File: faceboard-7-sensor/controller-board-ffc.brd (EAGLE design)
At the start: 51 x 42 mm, 7 parts, among them J1 DCJ0202

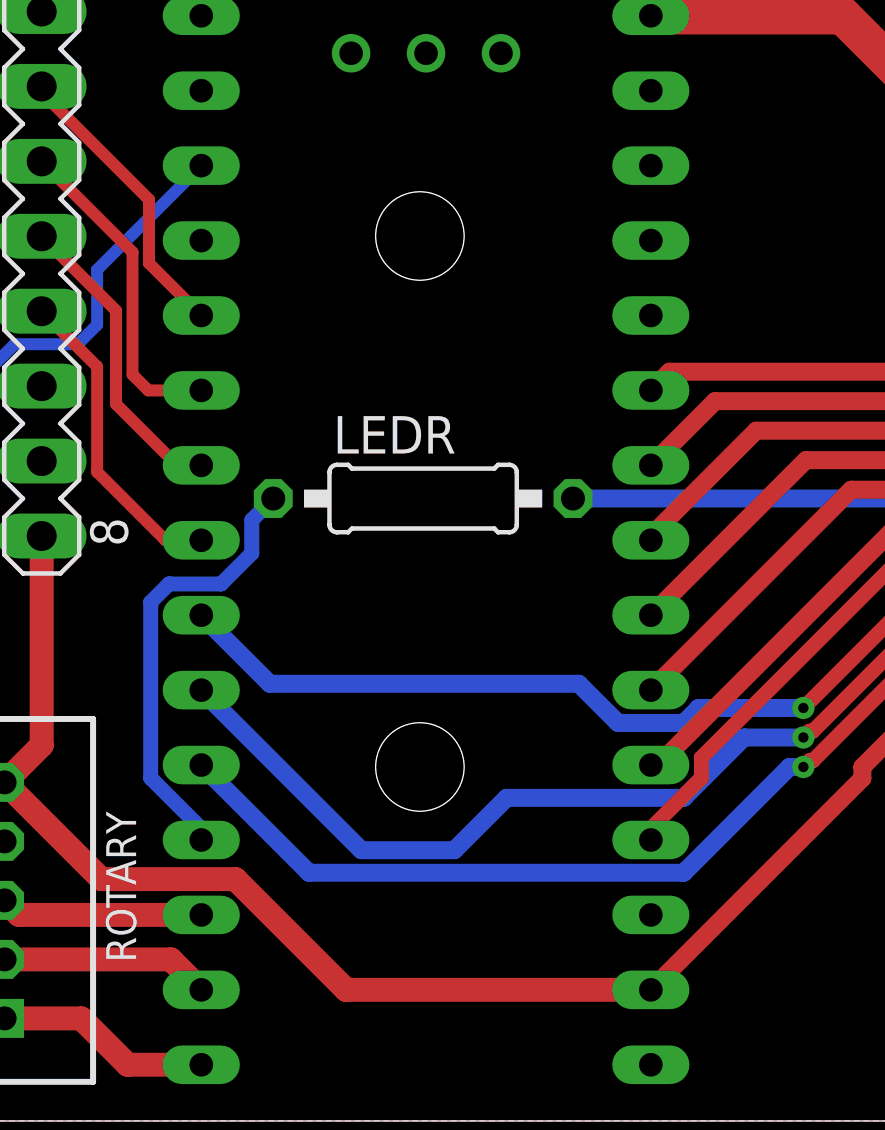
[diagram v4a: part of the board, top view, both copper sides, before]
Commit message: tidy silk screen
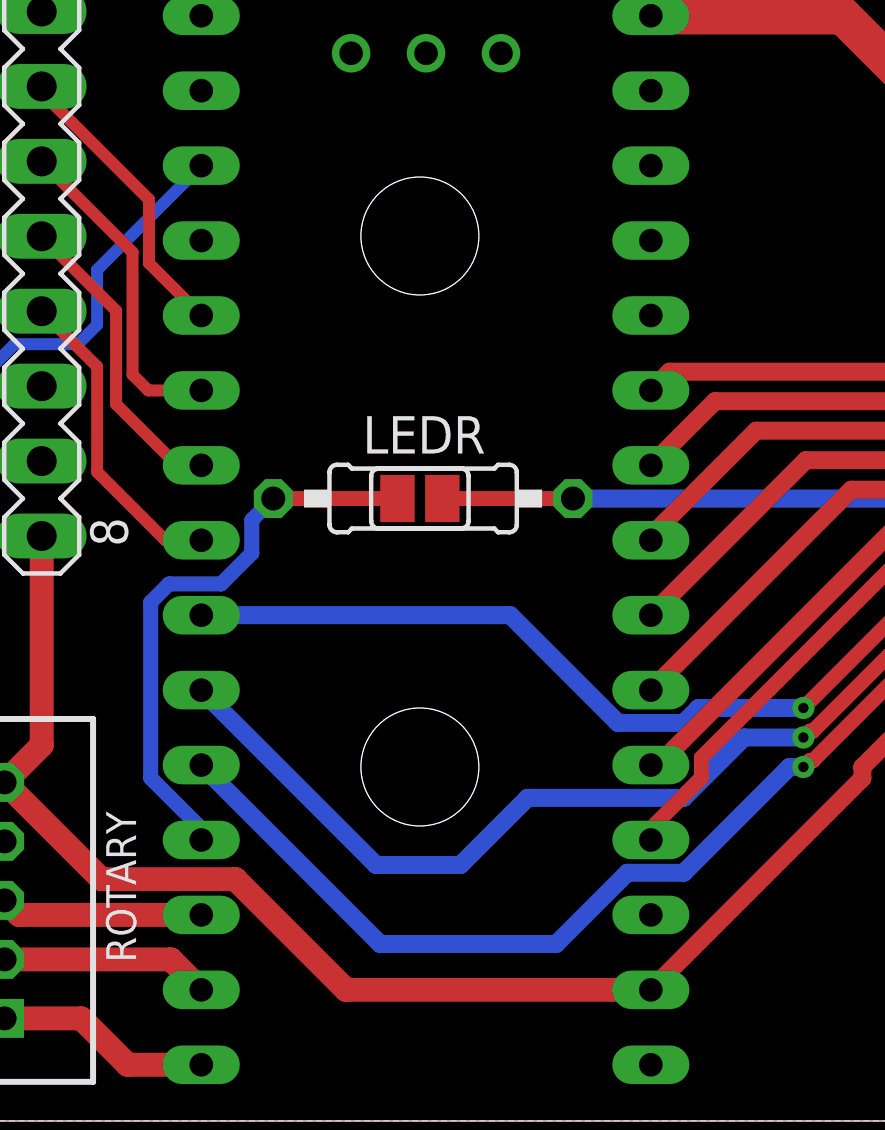
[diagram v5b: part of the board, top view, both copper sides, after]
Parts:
- added SJ1: (no value), jumper:SJ
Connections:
- net D9: now also SJ1.1
- net DIN: now also SJ1.2
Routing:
- net DIN: track 18.8 -> 23.2 mm
- net D9: track 15.0 -> 19.2 mm
- net A: track 29.0 -> 31.0 mm
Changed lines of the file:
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@@
 <layer number="97" name="Info" color="7" fill="1" visible="no" active="no"/>
 <layer number="98" name="Guide" color="6" fill="1" visible="no" active="no"/>
-<layer number="200" name="200bmp" color="1" fill="10" visible="yes" active="yes"/>
-<layer number="201" name="201bmp" color="2" fill="10" visible="yes" active="yes"/>
+<layer number="200" name="tBmp" color="1" fill="10" visible="yes" active="yes"/>
+<layer number="201" name="bBmp" color="2" fill="10" visible="yes" active="yes"/>
 <layer number="250" name="Descript" color="7" fill="1" visible="yes" active="yes"/>
 <layer number="251" name="SMDround" color="7" fill="1" visible="yes" active="yes"/>
@@
 <rectangle x1="1.005140625" y1="41.132178125" x2="8.004140625" y2="41.186859375" layer="201" rot="R180"/>
 <text x="21.7230375" y="1.03151875" size="0.5" layer="26" font="vector" rot="MR180">NEMUS Controller Board v0.1.3</text>
-<hole x="26" y="30" drill="3"/>
-<hole x="26" y="12" drill="3"/>
+<hole x="26" y="30" drill="4"/>
+<hole x="26" y="12" drill="4"/>
 </plain>
 <attributes>
@@
 <attribute name="OC_NEWARK" value="unknown" x="-30" y="-17" size="1.778" layer="27" rot="R270" display="off"/>
 <attribute name="POPULARITY" value="10" x="-30" y="-17" size="1.778" layer="27" rot="R270" display="off"/>
-<attribute name="VALUE" x="7.259" y="32.99" size="1.27" layer="27" ratio="10" rot="R270"/>
 </element>
 <element name="LEDR" library="rcl" library_urn="urn:adsk.eagle:library:334" package="0207/10" package3d_urn="urn:adsk.eagle:package:23491/2" value="300" x="26.11" y="21.1" smashed="yes">
-<attribute name="NAME" x="23.062" y="22.624" size="1.27" layer="25" ratio="10"/>
+<attribute name="NAME" x="24.062" y="22.624" size="1.27" layer="25" ratio="10"/>
 <attribute name="POPULARITY" value="81" x="60.4" y="-42.4" size="1.778" layer="27" display="off"/>
 <attribute name="SPICEPREFIX" value="R" x="60.4" y="-42.4" size="1.778" layer="27" display="off"/>
-<attribute name="VALUE" x="23.8494" y="20.465" size="1.27" layer="27" ratio="10"/>
 </element>
 <element name="ROTARY" library="con-jst-ph" package="B5B-PH-K" value="B5B-PH-K" x="11.921" y="7.477" smashed="yes" rot="R90">
 <attribute name="LABEL" value="" x="16.366" y="1.508" size="1.016" layer="25" ratio="18" rot="R90"/>
 <attribute name="NAME" x="15.365" y="10.492" size="1.016" layer="25" ratio="18" rot="R270"/>
-<attribute name="VALUE" x="13.826" y="2.397" size="1.016" layer="27" ratio="10" rot="R90"/>
 </element>
 <element name="U$1" library="Arduino-clone" package="NANO" value="NANO" x="23.669" y="28.575" smashed="yes" rot="R180"/>
@@
 <attribute name="MOUSER_PRICE-STOCK" value="https://www.mouser.co.uk/ProductDetail/Wurth-Elektronik/686114148922?qs=a9WhcLg8qCz0mPj5zZqo5g%3D%3D" x="46.2" y="18.9" size="1.778" layer="27" rot="R90" display="off"/>
 <attribute name="NAME" x="45.7" y="18.9" size="1.27" layer="25" rot="R90" align="center"/>
-<attribute name="VALUE" x="47.7" y="18.9" size="1.27" layer="27" rot="R90" align="center"/>
 </element>
 <element name="J1" library="con-jack" library_urn="urn:adsk.eagle:library:154" package="DCJ0202" package3d_urn="urn:adsk.eagle:package:7491/1" value="DCJ0202" x="45.9" y="35" smashed="yes" rot="R90">
@@
 <attribute name="OC_NEWARK" value="unknown" x="45.9" y="35" size="1.778" layer="27" rot="R90" display="off"/>
 <attribute name="POPULARITY" value="17" x="45.9" y="35" size="1.778" layer="27" rot="R90" display="off"/>
-<attribute name="VALUE" x="40.92" y="31.94" size="1.27" layer="27" rot="R90"/>
 </element>
 <element name="RESET" library="con-jst-ph" package="B2B-PH-K" value="B2B-PH-K" x="6.2" y="10.5" smashed="yes" rot="R270">
 <attribute name="LABEL" value="" x="6.2" y="10.5" size="1.778" layer="27" rot="R270" display="off"/>
 <attribute name="NAME" x="9.514" y="8.579" size="1.016" layer="25" ratio="18" rot="R90"/>
-<attribute name="VALUE" x="1.295" y="13.405" size="1.016" layer="27" ratio="10" rot="R270"/>
+</element>
+<element name="SJ1" library="jumper" library_urn="urn:adsk.eagle:library:252" package="SJ" package3d_urn="urn:adsk.eagle:package:15471/1" value="" x="26" y="21.1" smashed="yes">
+<attribute name="POPULARITY" value="33" x="26" y="21.1" size="1.778" layer="27" display="off"/>
+<attribute name="VALUE" x="26.4001" y="21.1" size="0.02" layer="27"/>
 </element>
 </elements>
@@
 <wire x1="38.529475" y1="12" x2="39" y2="12" width="0.6096" layer="16"/>
 <wire x1="34.943275" y1="8.4138" x2="38.529475" y2="12" width="0.6096" layer="16"/>
-<wire x1="18.589" y1="12.065" x2="22.2402" y2="8.4138" width="0.6096" layer="16"/>
-<wire x1="22.2402" y1="8.4138" x2="34.943275" y2="8.4138" width="0.6096" layer="16"/>
 <wire x1="39" y1="12" x2="39.2154" y2="12.2154" width="0.508" layer="1"/>
 <wire x1="39.2154" y1="12.2154" x2="39.32499375" y2="12.2154" width="0.508" layer="1"/>
 <wire x1="42.50959375" y1="15.4" x2="43.15" y2="15.4" width="0.508" layer="1"/>
 <wire x1="39.32499375" y1="12.2154" x2="42.50959375" y2="15.4" width="0.508" layer="1"/>
+<wire x1="18.589" y1="12.065" x2="24.654" y2="6" width="0.6096" layer="16"/>
+<wire x1="30.618525" y1="6" x2="33.032325" y2="8.4138" width="0.6096" layer="16"/>
+<wire x1="24.654" y1="6" x2="30.618525" y2="6" width="0.6096" layer="16"/>
+<wire x1="33.032325" y1="8.4138" x2="34.943275" y2="8.4138" width="0.6096" layer="16"/>
 </signal>
 <signal name="B">
@@
 <contactref element="RIBBON1" pad="5"/>
 <via x="39" y="13" extent="1-16" drill="0.35"/>
-<wire x1="27.16841875" y1="9.1792" x2="28.94301875" y2="10.9538" width="0.6096" layer="16"/>
 <wire x1="36.989475" y1="13" x2="39" y2="13" width="0.6096" layer="16"/>
-<wire x1="28.94301875" y1="10.9538" x2="34.943275" y2="10.9538" width="0.6096" layer="16"/>
 <wire x1="34.943275" y1="10.9538" x2="36.989475" y2="13" width="0.6096" layer="16"/>
-<wire x1="18.589" y1="14.605" x2="24.0148" y2="9.1792" width="0.6096" layer="16"/>
-<wire x1="24.0148" y1="9.1792" x2="27.16841875" y2="9.1792" width="0.6096" layer="16"/>
 <wire x1="39" y1="13" x2="39.2154" y2="13.2154" width="0.508" layer="1"/>
 <wire x1="39.2154" y1="13.2154" x2="39.32499375" y2="13.2154" width="0.508" layer="1"/>
 <wire x1="42.50959375" y1="16.4" x2="43.15" y2="16.4" width="0.508" layer="1"/>
 <wire x1="39.32499375" y1="13.2154" x2="42.50959375" y2="16.4" width="0.508" layer="1"/>
+<wire x1="27.375525" y1="8.6792" x2="29.650125" y2="10.9538" width="0.6096" layer="16"/>
+<wire x1="18.589" y1="14.605" x2="24.5148" y2="8.6792" width="0.6096" layer="16"/>
+<wire x1="24.5148" y1="8.6792" x2="27.375525" y2="8.6792" width="0.6096" layer="16"/>
+<wire x1="29.650125" y1="10.9538" x2="34.943275" y2="10.9538" width="0.6096" layer="16"/>
 </signal>
 <signal name="C">
@@
 <wire x1="34.943275" y1="13.4938" x2="35.449475" y2="14" width="0.6096" layer="16"/>
 <wire x1="35.449475" y1="14" x2="39" y2="14" width="0.6096" layer="16"/>
-<wire x1="18.589" y1="17.145" x2="20.9132" y2="14.8208" width="0.6096" layer="16"/>
-<wire x1="20.9132" y1="14.8208" x2="31.387725" y2="14.8208" width="0.6096" layer="16"/>
-<wire x1="31.387725" y1="14.8208" x2="32.714725" y2="13.4938" width="0.6096" layer="16"/>
 <wire x1="39" y1="14" x2="42.4" y2="17.4" width="0.508" layer="1"/>
 <wire x1="42.4" y1="17.4" x2="43.15" y2="17.4" width="0.508" layer="1"/>
+<wire x1="18.589" y1="17.145" x2="29.063525" y2="17.145" width="0.6096" layer="16"/>
+<wire x1="29.063525" y1="17.145" x2="32.714725" y2="13.4938" width="0.6096" layer="16"/>
 </signal>
 <signal name="RST">
@@
 <wire x1="43.15" y1="18.4" x2="44.4" y2="18.4" width="0.508" layer="1"/>
 <wire x1="44.4" y1="18.4" x2="46" y2="20" width="0.508" layer="1"/>
+<contactref element="SJ1" pad="2"/>
+<wire x1="26.762" y1="21.1" x2="31.19" y2="21.1" width="0.508" layer="1"/>
 </signal>
 <signal name="VCC">
@@
 <wire x1="19.2630375" y1="18.2054" x2="17.4957625" y2="18.2054" width="0.508" layer="16"/>
 <wire x1="16.8746" y1="17.5842375" x2="16.8746" y2="11.6257625" width="0.508" layer="16"/>
+<contactref element="SJ1" pad="1"/>
+<wire x1="21.03" y1="21.1" x2="25.238" y2="21.1" width="0.508" layer="1"/>
 </signal>
 <signal name="RC">
